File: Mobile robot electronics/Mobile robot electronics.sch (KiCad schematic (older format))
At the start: 41 parts, among them J1 Front_Sens, J10 Conn_01x06_Male, J2 Back_Sens, J3 Left_Sens, J4 Right_sens, J5 Conn_01x02_Male, J6 Conn_01x02_Male, J7 Conn_01x06_Male, J8 Conn_01x06_Male, J9 Conn_01x06_Male, U1 ESP32-DevKitc-V4-WROVER, U2 BD65496MUV, U3 BD65496MUV, U4 BD65496MUV, U5 BD65496MUV

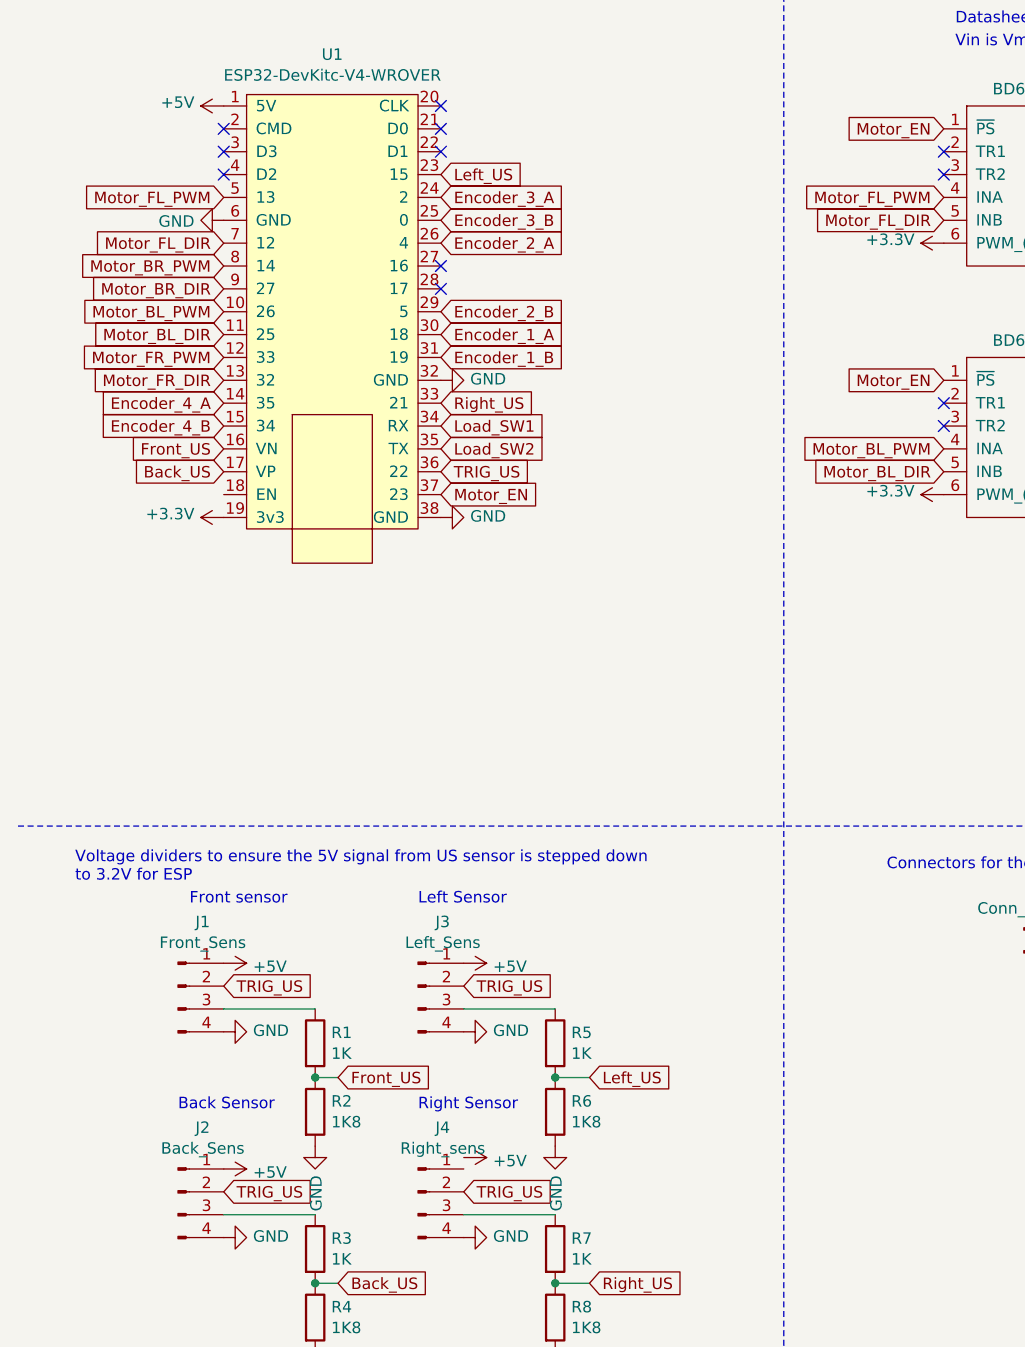
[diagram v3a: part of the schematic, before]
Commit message: routed tracks for pcb, changed some pins on esp
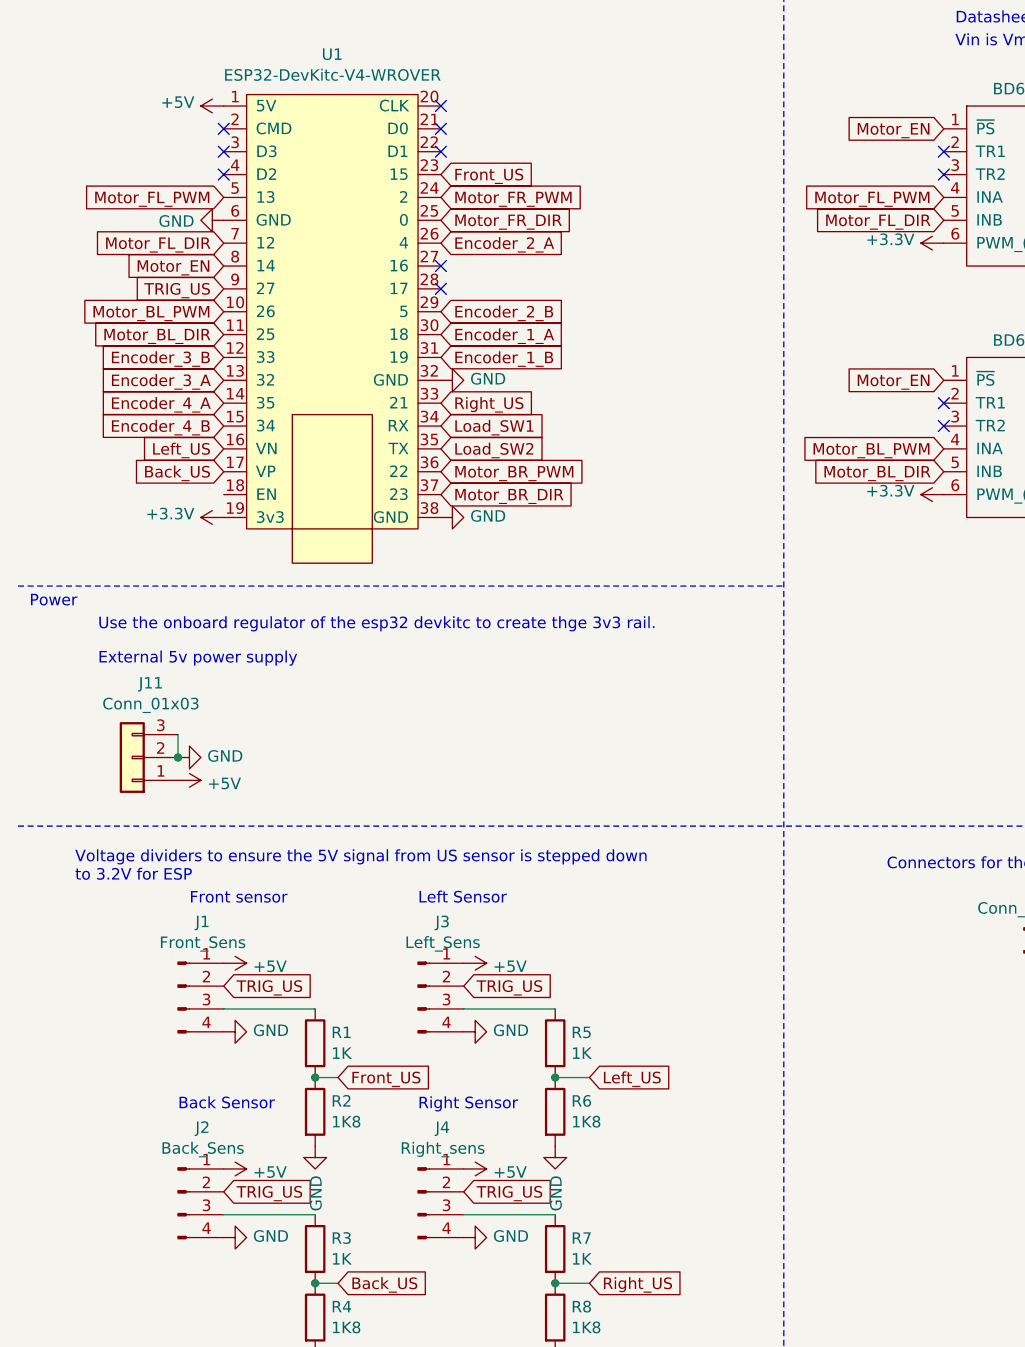
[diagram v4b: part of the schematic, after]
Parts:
- added J11: Conn_01x03, Connector_BarrelJack:BarrelJack_Horizontal, symbol Connector_Generic:Conn_01x03
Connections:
- net +5V: now also J4.1 (Pin_1), J11.1 (Pin_1)
- net Encoder_3_A: now also U1.13 (32); no longer U1.24 (2)
- net Encoder_3_B: now also U1.12 (33); no longer U1.25 (0)
- net Front_US: now also U1.23 (15); no longer U1.16 (VN)
- net GND: now also J11.2 (Pin_2), J11.3 (Pin_3)
- net Left_US: now also U1.16 (VN); no longer U1.23 (15)
- net Motor_BR_DIR: now also U1.37 (23); no longer U1.9 (27)
- net Motor_BR_PWM: now also U1.36 (22); no longer U1.8 (14)
- net Motor_EN: now also U1.8 (14); no longer U1.37 (23)
- net Motor_FR_DIR: now also U1.25 (0); no longer U1.13 (32)
- net Motor_FR_PWM: now also U1.24 (2); no longer U1.12 (33)
- net TRIG_US: now also U1.9 (27); no longer U1.36 (22)
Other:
- note added: "External 5v power supply\n"
- note added: "Power\n"
- note added: "Use the onboard regulator of the esp32 devkitc to create thge 3v3 rail."
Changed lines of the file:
@@
 Text GLabel 6600 1500 0    50   Input ~ 0
 Motor_FR_PWM
-Text GLabel 2300 2800 2    50   Input ~ 0
+Text GLabel 1350 1800 0    50   Input ~ 0
 Motor_EN
 Text Notes 500  550  0    50   ~ 0
@@
 Text Notes 8000 550  0    50   ~ 0
 Motor Connectors
-Text GLabel 2300 1600 2    50   Input ~ 0
+Text GLabel 1350 2200 0    50   Input ~ 0
 Encoder_3_B
 Text GLabel 2300 2100 2    50   Input ~ 0
@@
 L power:+5V #PWR0137
 U 1 1 6075120E
-P 2400 5700
-F 0 "#PWR0137" H 2400 5550 50  0001 C CNN
-F 1 "+5V" V 2415 5828 50  0000 L CNN
-F 2 "" H 2400 5700 50  0001 C CNN
-F 3 "" H 2400 5700 50  0001 C CNN
-	1    2400 5700
+P 2400 5750
+F 0 "#PWR0137" H 2400 5600 50  0001 C CNN
+F 1 "+5V" V 2415 5878 50  0000 L CNN
+F 2 "" H 2400 5750 50  0001 C CNN
+F 3 "" H 2400 5750 50  0001 C CNN
+	1    2400 5750
 	0    1    1    0
 $EndComp
@@
 	0    -1   -1   0
 $EndComp
-Text GLabel 2300 1500 2    50   Input ~ 0
+Text GLabel 1350 2300 0    50   Input ~ 0
 Encoder_3_A
 Text GLabel 6600 1600 0    50   Input ~ 0
@@
 Text GLabel 1350 1700 0    50   Input ~ 0
 Motor_FL_DIR
-Text GLabel 1350 2200 0    50   Input ~ 0
+Text GLabel 2300 1500 2    50   Input ~ 0
 Motor_FR_PWM
-Text GLabel 1350 2300 0    50   Input ~ 0
+Text GLabel 2300 1600 2    50   Input ~ 0
 Motor_FR_DIR
 Text GLabel 1350 2000 0    50   Input ~ 0
@@
 Text GLabel 1350 2100 0    50   Input ~ 0
 Motor_BL_DIR
-Text GLabel 1350 1800 0    50   Input ~ 0
+Text GLabel 2300 2700 2    50   Input ~ 0
 Motor_BR_PWM
-Text GLabel 1350 1900 0    50   Input ~ 0
+Text GLabel 2300 2800 2    50   Input ~ 0
 Motor_BR_DIR
 $Comp
@@
 Text GLabel 2400 5850 2    50   Input ~ 0
 TRIG_US
-Text GLabel 2300 2700 2    50   Input ~ 0
+Text GLabel 1350 1900 0    50   Input ~ 0
 TRIG_US
 Text Notes 1200 4600 0    50   ~ 0
@@
 	2800 6250 2950 6250
 Connection ~ 2800 6250
-Text GLabel 1350 2600 0    50   Input ~ 0
+Text GLabel 2300 1400 2    50   Input ~ 0
 Front_US
 Text GLabel 1350 2700 0    50   Input ~ 0
 Back_US
-Text GLabel 2300 1400 2    50   Input ~ 0
+Text GLabel 1350 2600 0    50   Input ~ 0
 Left_US
 Text GLabel 2300 2400 2    50   Input ~ 0
@@
 Text GLabel 2300 2500 2    50   Input ~ 0
 Load_SW1
+Text Notes 800  3400 0    50   ~ 0
+Use the onboard regulator of the esp32 devkitc to create thge 3v3 rail.
+Text Notes 800  3550 0    50   ~ 0
+External 5v power supply\n
+Wire Notes Line
+	450  3200 3800 3200
+Text Notes 500  3300 0    50   ~ 0
+Power\n
+$Comp
+L power:GND #PWR0150
+U 1 1 608EA124
+P 1150 3950
+F 0 "#PWR0150" H 1150 3700 50  0001 C CNN
+F 1 "GND" V 1155 3822 50  0000 R CNN
+F 2 "" H 1150 3950 50  0001 C CNN
+F 3 "" H 1150 3950 50  0001 C CNN
+	1    1150 3950
+	0    -1   -1   0
+$EndComp
+$Comp
+L power:+5V #PWR0151
+U 1 1 608EAA30
+P 1150 4050
+F 0 "#PWR0151" H 1150 3900 50  0001 C CNN
+F 1 "+5V" V 1165 4178 50  0000 L CNN
+F 2 "" H 1150 4050 50  0001 C CNN
+F 3 "" H 1150 4050 50  0001 C CNN
+	1    1150 4050
+	0    1    1    0
+$EndComp
+$Comp
+L Connector_Generic:Conn_01x03 J11
+U 1 1 608EC567
+P 950 3950
+F 0 "J11" H 868 3625 50  0000 C CNN
+F 1 "Conn_01x03" H 868 3716 50  0000 C CNN
+F 2 "Connector_BarrelJack:BarrelJack_Horizontal" H 950 3950 50  0001 C CNN
+F 3 "~" H 950 3950 50  0001 C CNN
+	1    950  3950
+	-1   0    0    1
+$EndComp
+Wire Wire Line
+	1150 3850 1150 3950
+Connection ~ 1150 3950
 $EndSCHEMATC

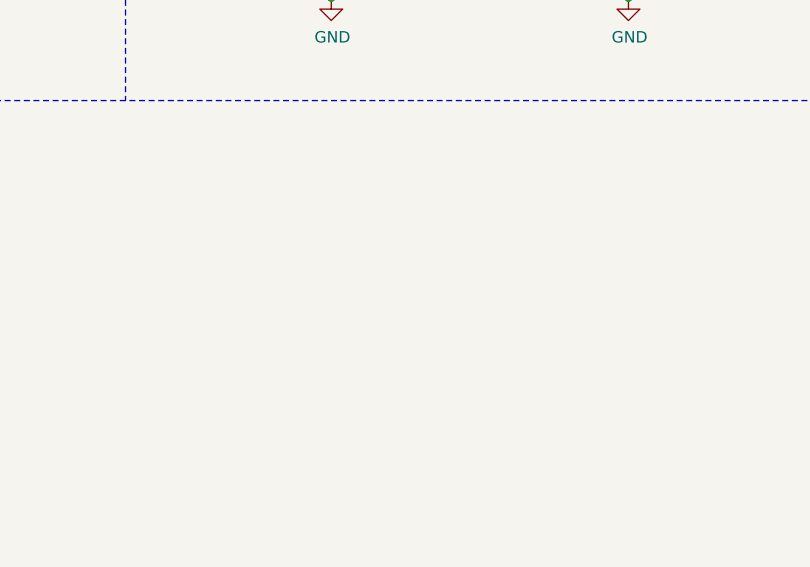
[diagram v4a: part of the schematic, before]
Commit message: added mounting holes for PCB
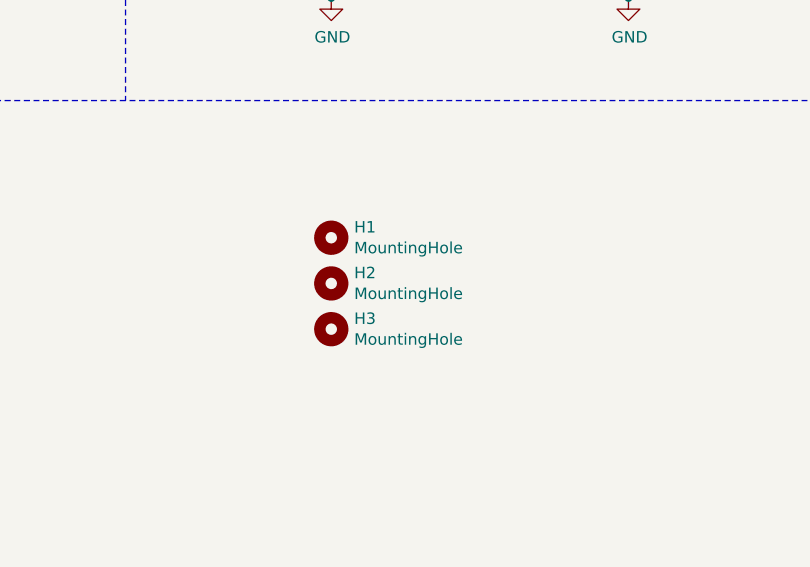
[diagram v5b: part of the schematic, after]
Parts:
- added H1, H2, H3: MountingHole, MountingHole:MountingHole_4.3mm_M4, symbol Mechanical:MountingHole
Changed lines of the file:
@@
 	1150 3850 1150 3950
 Connection ~ 1150 3950
+$Comp
+L Mechanical:MountingHole H1
+U 1 1 6088D218
+P 8850 4850
+F 0 "H1" H 8950 4896 50  0000 L CNN
+F 1 "MountingHole" H 8950 4805 50  0000 L CNN
+F 2 "MountingHole:MountingHole_4.3mm_M4" H 8850 4850 50  0001 C CNN
+F 3 "~" H 8850 4850 50  0001 C CNN
+	1    8850 4850
+	1    0    0    -1
+$EndComp
+$Comp
+L Mechanical:MountingHole H2
+U 1 1 6088D7F9
+P 8850 5050
+F 0 "H2" H 8950 5096 50  0000 L CNN
+F 1 "MountingHole" H 8950 5005 50  0000 L CNN
+F 2 "MountingHole:MountingHole_4.3mm_M4" H 8850 5050 50  0001 C CNN
+F 3 "~" H 8850 5050 50  0001 C CNN
+	1    8850 5050
+	1    0    0    -1
+$EndComp
+$Comp
+L Mechanical:MountingHole H3
+U 1 1 6088E0B9
+P 8850 5250
+F 0 "H3" H 8950 5296 50  0000 L CNN
+F 1 "MountingHole" H 8950 5205 50  0000 L CNN
+F 2 "MountingHole:MountingHole_4.3mm_M4" H 8850 5250 50  0001 C CNN
+F 3 "~" H 8850 5250 50  0001 C CNN
+	1    8850 5250
+	1    0    0    -1
+$EndComp
 $EndSCHEMATC
